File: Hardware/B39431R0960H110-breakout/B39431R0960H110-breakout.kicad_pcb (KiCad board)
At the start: 2 copper layers, 12 x 9.5 mm, 4 parts, among them J1 Conn_Coaxial_x2, U1 RF1404D

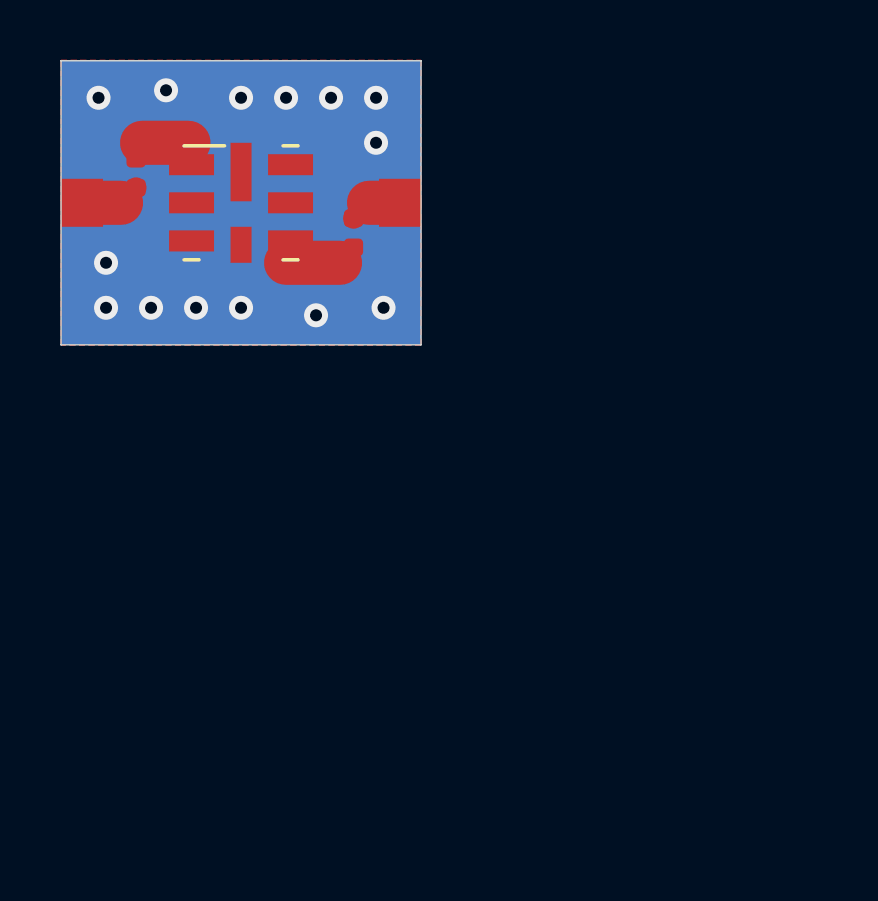
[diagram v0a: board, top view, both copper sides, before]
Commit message: SAW Breakout: DRC ERC Pass
Ready for PR
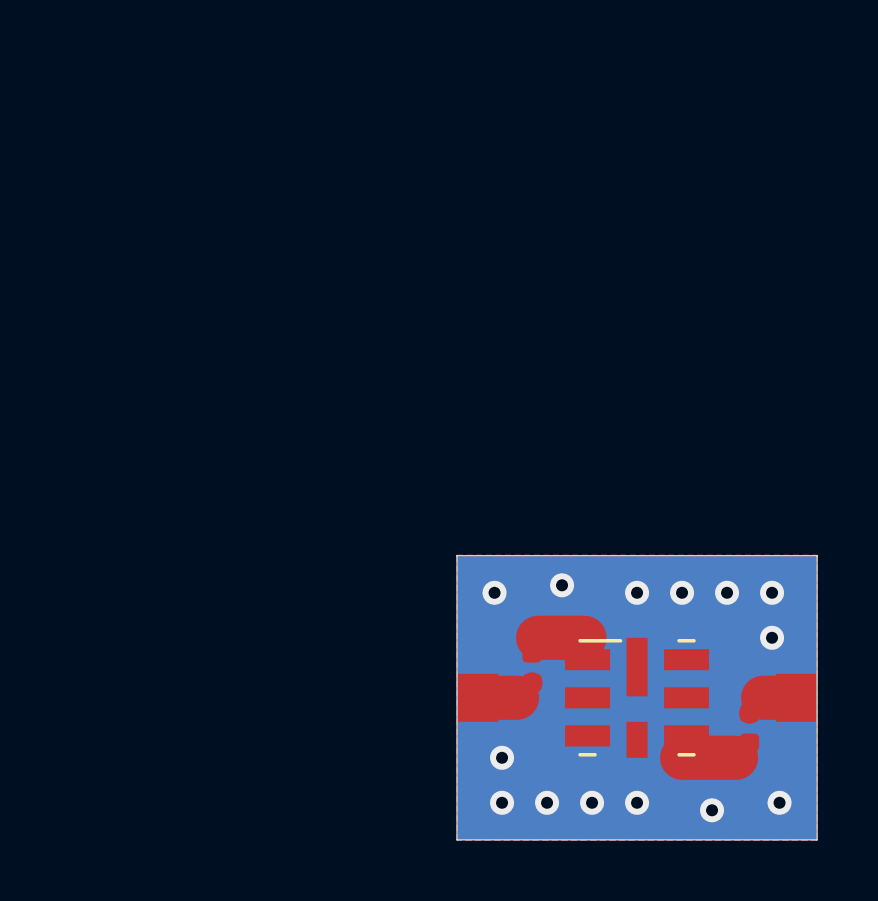
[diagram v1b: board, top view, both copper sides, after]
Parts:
- moved J1 21.1 mm to (132.2, 102.0)
- moved L1 21.1 mm to (128.7, 101.0)
- moved L2 21.1 mm to (135.9, 103.0)
- moved U1 21.1 mm to (132.2, 102.0)
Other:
- board text added: "1.8mm FR4 Dk = 4.5 Green Soldermask No Silkscreen HASL Lead Free Order with Stencil"
